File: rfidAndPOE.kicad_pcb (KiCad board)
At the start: 2 copper layers, 122 parts, among them J1 0813-1X1T-57-F, J2 SWD, J3 MCU Port B, J4 MCU Port C, P1 PoE-, P2 PoE+, P3 GND, P4 +5V, P5 +12V, P6 +3V3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

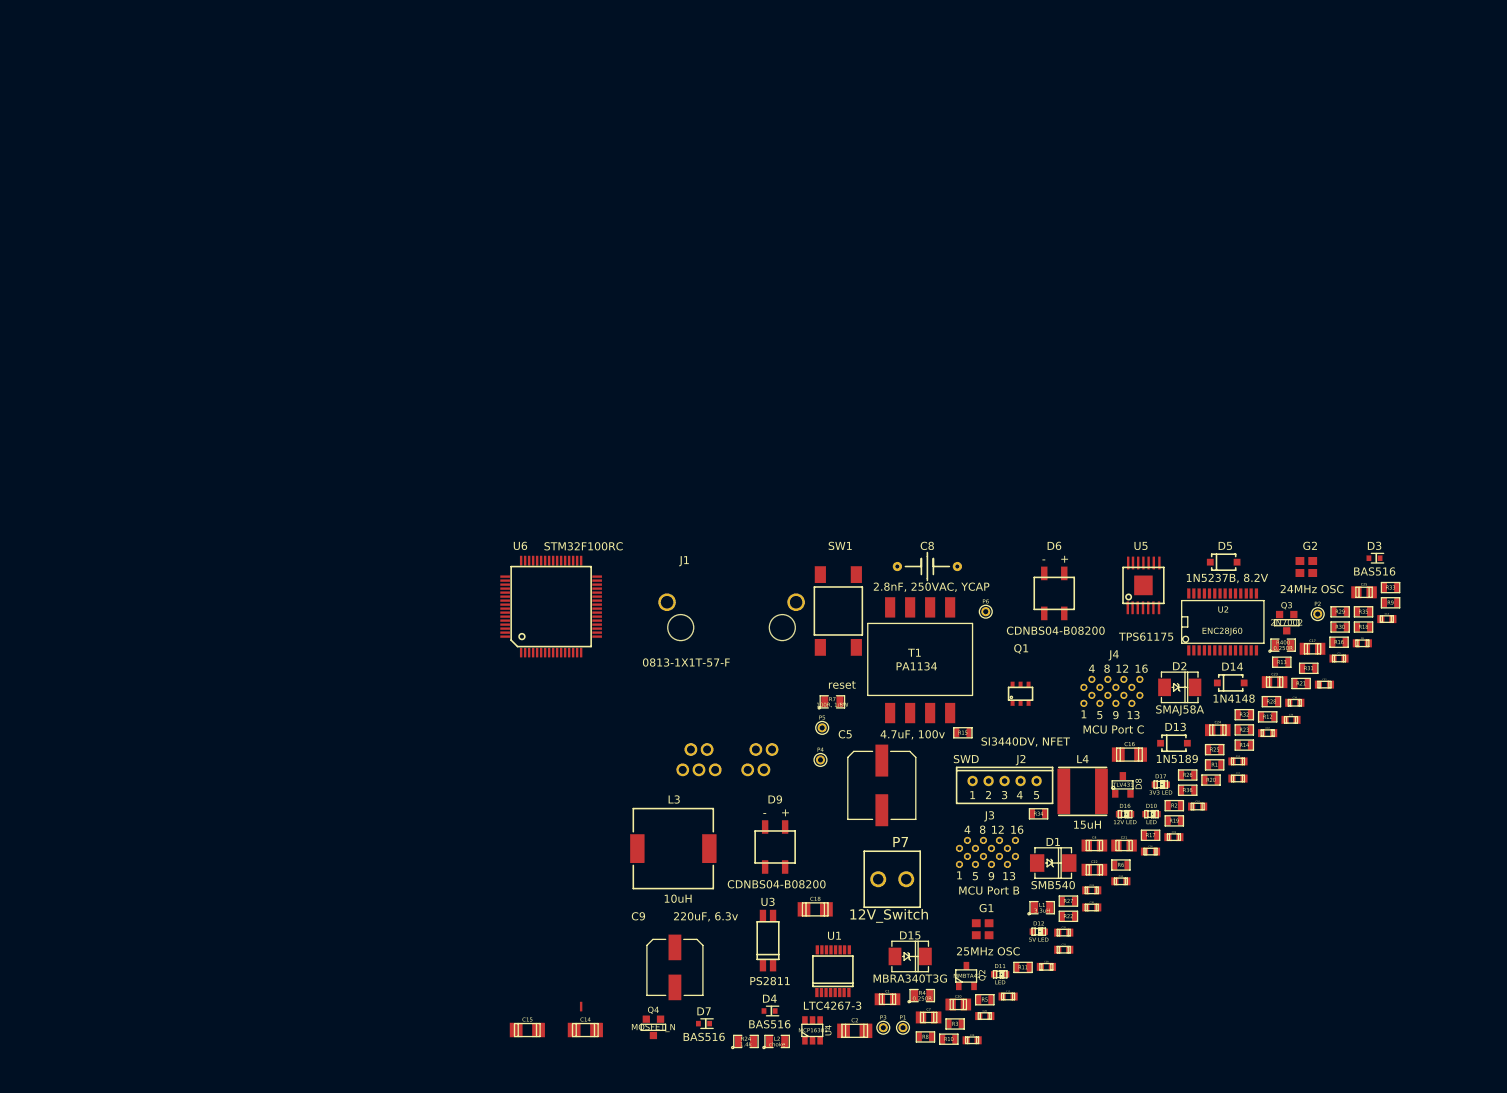
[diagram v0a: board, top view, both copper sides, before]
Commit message: Added 3.1mm mounting holes for M3 bolts. Started positioning some components.
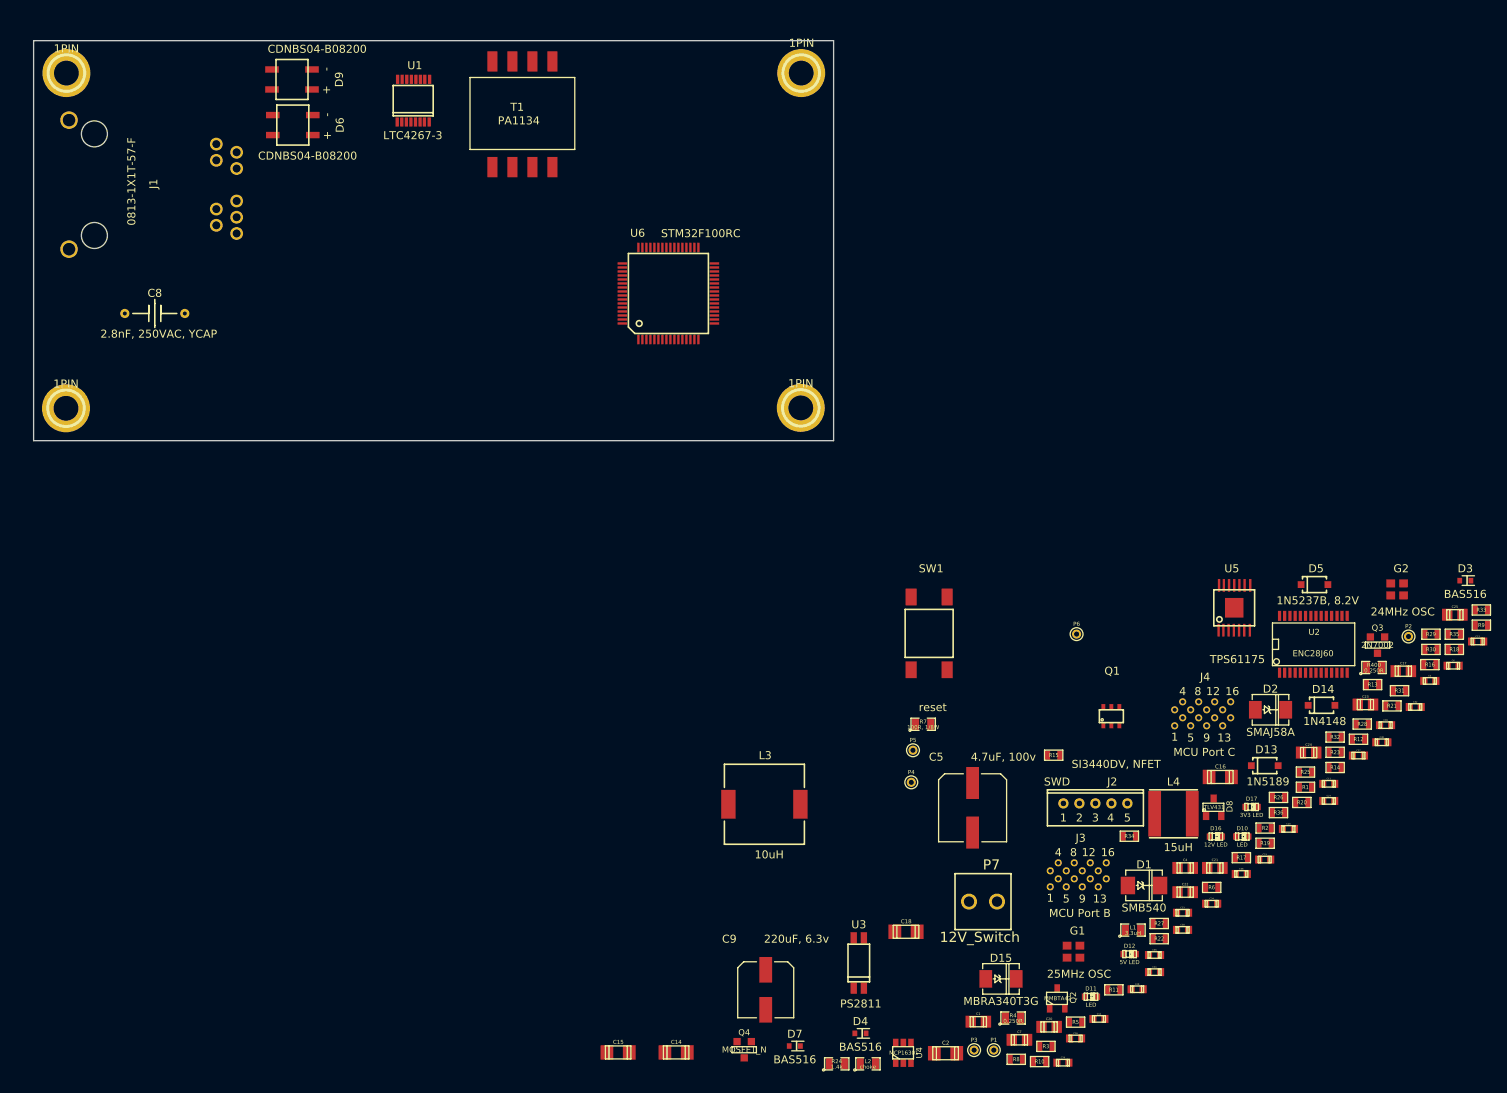
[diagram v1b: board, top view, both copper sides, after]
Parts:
- added 1PIN: P***, Connect:1pin, F.Cu at (173.8, 34.8)
- added 1PIN: P***, Connect:1pin, F.Cu at (81.8, 76.7)
- added 1PIN: P***, Connect:1pin, F.Cu at (173.7, 76.6)
- added 1PIN: P***, Connect:1pin, F.Cu at (81.9, 34.8)
- moved U1 120.8 mm to (125.2, 38.2)
- moved D9 113.4 mm to (110.1, 35.5), turned to 270 degrees
- moved D6 111.7 mm to (110.2, 41.2), turned to 270 degrees
- moved C8 101.6 mm to (93.0, 64.8)
- moved J1 88.2 mm to (85.4, 55.0), turned to 90 degrees
- moved T1 84.4 mm to (135.2, 46.5)
- moved U6 41.8 mm to (157.2, 62.3)
- moved L3 12.7 mm to (169.2, 126.2)
- moved C27 11.7 mm to (239.7, 125.7)
- moved C31 11.7 mm to (217.9, 147.1)
- moved C38 11.7 mm to (221.4, 141.9)
- moved D1 11.7 mm to (216.6, 136.3)
- moved D7 11.7 mm to (173.0, 156.4)
- moved P7 11.7 mm to (196.5, 138.3)
- moved R12 11.7 mm to (243.4, 118.0)
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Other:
- board outline added: 100 x 50 mm

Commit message: Moved ethernet port in to position and started routing some of the PoE stuff. Started moving other components near where they may end up going.,
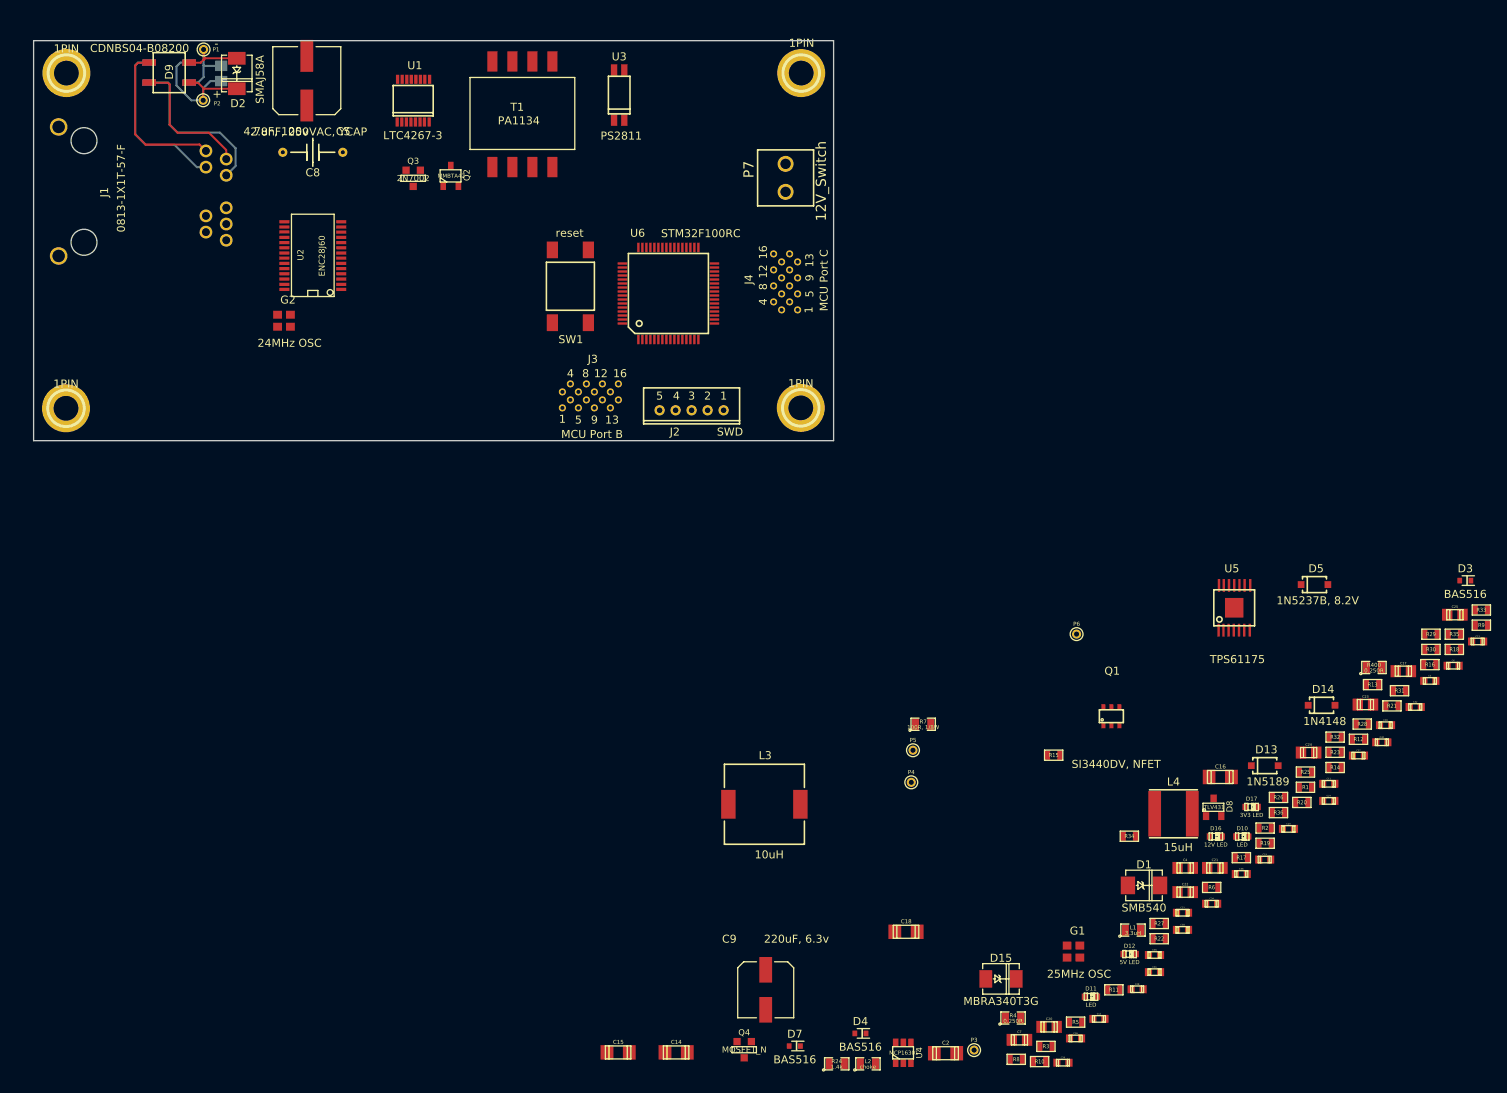
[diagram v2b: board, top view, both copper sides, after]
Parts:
- C1, D6: moved to B.Cu
- moved P2 164.9 mm to (99.0, 38.1)
- moved P1 159.4 mm to (99.0, 31.8)
- moved D2 151.7 mm to (103.2, 34.8), turned to 270 degrees
- moved C1 151.7 mm to (101.2, 34.8), turned to 270 degrees
- moved G2 143.1 mm to (109.1, 65.7)
- moved U2 134.1 mm to (112.7, 57.6), turned to 90 degrees
- moved Q3 133.9 mm to (125.2, 47.9)
- moved Q2 127.7 mm to (129.9, 47.6)
- moved C5 123.2 mm to (112.0, 35.7), turned to 180 degrees
- moved U3 112.5 mm to (151.0, 37.5)
- moved P7 93.8 mm to (171.8, 47.9), turned to 90 degrees
- moved J3 85.5 mm to (148.9, 75.6)
- moved J4 77.2 mm to (172.3, 59.4), turned to 90 degrees
- moved J2 70.4 mm to (160.1, 76.9), turned to 180 degrees
- moved SW1 62.4 mm to (144.9, 61.4), turned to 180 degrees
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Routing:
- net /Ethernet-: track 0.00 -> 21.0 mm
- net /Ethernet+: track 0.00 -> 21.0 mm
- net Net-(C1-Pad1): track 0.00 -> 20.2 mm
- net /EthernetSpare+: track 0.00 -> 20.2 mm
- net /EthernetSpare-: track 0.00 -> 17.2 mm
- net Net-(C1-Pad2): track 0.00 -> 15.2 mm
